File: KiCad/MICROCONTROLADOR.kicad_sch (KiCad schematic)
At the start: 18 parts, among them J3 Screw_Terminal_01x05, SW8 SW_Push, U67 PIC24HJ64GP504-I/PT, Y1 8 MHz

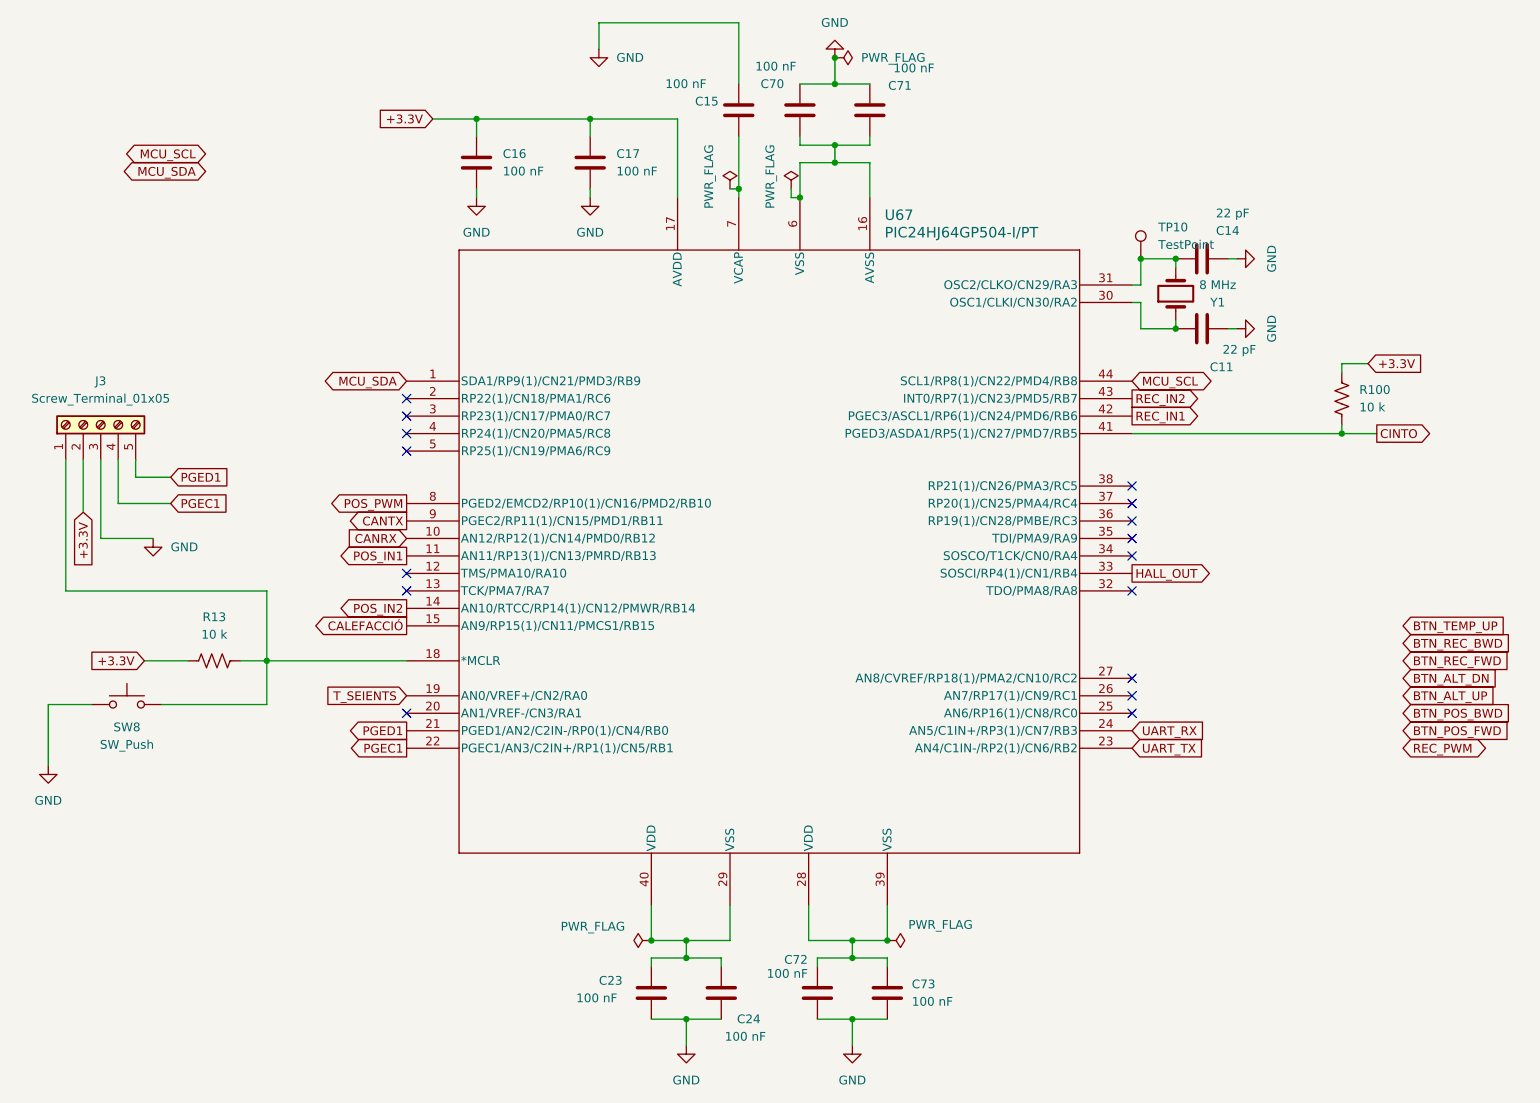
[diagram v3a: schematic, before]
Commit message: Organització Esquematic, asignacio huellas Test Points i Microcontrolador acabat
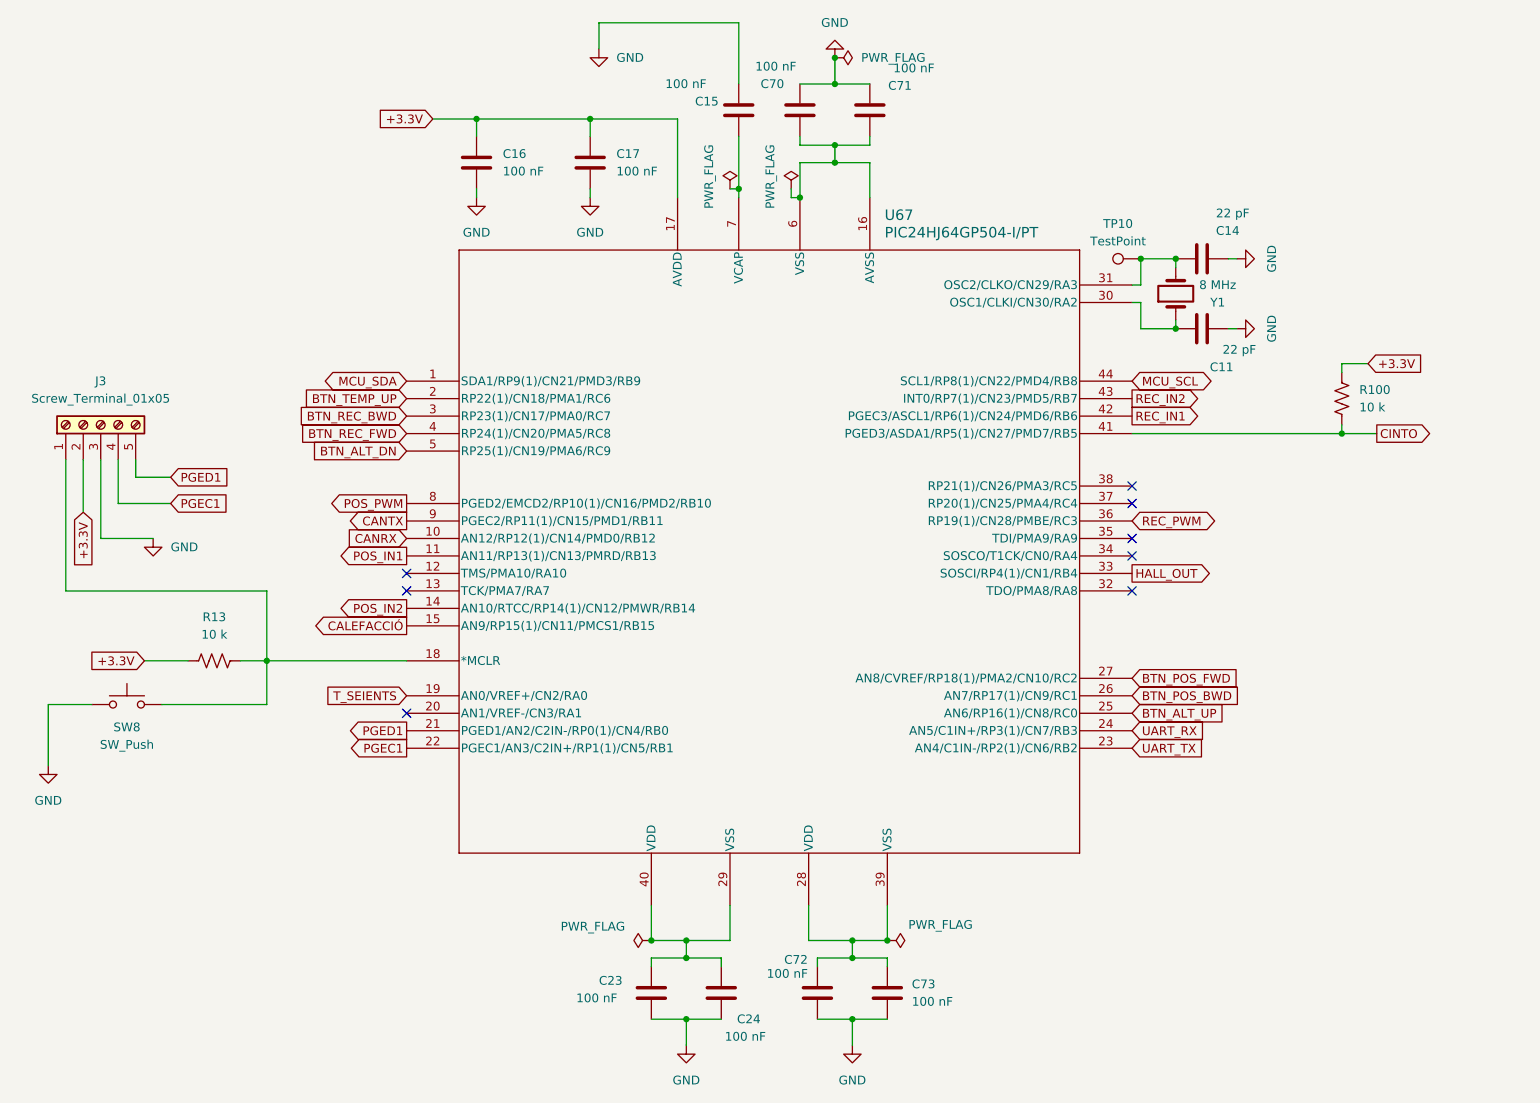
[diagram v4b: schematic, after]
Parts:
- TP10: footprint (none) -> TestPoint:TestPoint_Pad_D1.0mm
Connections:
- net BTN_ALT_DN: now also U67.5 (RP25(1)/CN19/PMA6/RC9)
- net BTN_ALT_UP: now also U67.25 (AN6/RP16(1)/CN8/RC0)
- net BTN_POS_BWD: now also U67.26 (AN7/RP17(1)/CN9/RC1)
- net BTN_POS_FWD: now also U67.27 (AN8/CVREF/RP18(1)/PMA2/CN10/RC2)
- net BTN_REC_BWD: now also U67.3 (RP23(1)/CN17/PMA0/RC7)
- net BTN_REC_FWD: now also U67.4 (RP24(1)/CN20/PMA5/RC8)
- net BTN_TEMP_UP: now also U67.2 (RP22(1)/CN18/PMA1/RC6)
- net REC_PWM: now also U67.36 (RP19(1)/CN28/PMBE/RC3)
- no-connect marks 16 -> 8
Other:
- moved on the sheet: TP10
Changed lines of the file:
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@@
 	)
 	(no_connect
-		(at 100.33 78.74)
+		(at 205.74 83.82)
+	)
+	(no_connect
+		(at 100.33 96.52)
+	)
+	(no_connect
+		(at 100.33 116.84)
 	)
 	(no_connect
@@
 	)
 	(no_connect
+		(at 205.74 93.98)
+	)
+	(no_connect
+		(at 205.74 86.36)
+	)
+	(no_connect
 		(at 100.33 99.06)
-	)
-	(no_connect
-		(at 100.33 116.84)
 	)
 	(no_connect
 		(at 205.74 99.06)
 	)
-	(no_connect
-		(at 205.74 83.82)
-	)
-	(no_connect
-		(at 205.74 86.36)
-	)
-	(no_connect
-		(at 100.33 96.52)
-	)
-	(no_connect
-		(at 205.74 114.3)
-	)
-	(no_connect
-		(at 100.33 73.66)
-	)
-	(no_connect
-		(at 100.33 76.2)
-	)
-	(no_connect
-		(at 205.74 111.76)
-	)
-	(no_connect
-		(at 205.74 116.84)
-	)
-	(no_connect
-		(at 205.74 88.9)
-	)
-	(no_connect
-		(at 100.33 71.12)
-	)
-	(no_connect
-		(at 205.74 93.98)
-	)
 	(wire
 		(pts
@@
 			(width 0)
 			(type default)
-		)
-	)
-	(global_label "MCU_SDA"
-		(shape bidirectional)
-		(at 71.12 38.1 180)
-		(fields_autoplaced yes)
-		(effects
-			(font
-				(size 1.27 1.27)
-			)
-			(justify right)
-		)
-		(property "Intersheetrefs" "${INTERSHEET_REFS}"
-			(at 58.4359 38.1 0)
-			(effects
-				(font
-					(size 1.27 1.27)
-				)
-				(justify right)
-				(hide yes)
-			)
 		)
 	)
@@
 	(global_label "BTN_POS_FWD"
 		(shape input)
-		(at 245.11 119.38 0)
+		(at 205.74 111.76 0)
 		(fields_autoplaced yes)
 		(effects
@@
 		)
 		(property "Intersheetrefs" "${INTERSHEET_REFS}"
-			(at 260.5643 119.38 0)
+			(at 221.1943 111.76 0)
 			(effects
 				(font
@@
 	(global_label "BTN_TEMP_UP"
 		(shape input)
-		(at 245.11 104.14 0)
-		(fields_autoplaced yes)
-		(effects
-			(font
-				(size 1.27 1.27)
-			)
-			(justify left)
-		)
-		(property "Intersheetrefs" "${INTERSHEET_REFS}"
-			(at 260.3828 104.14 0)
-			(effects
-				(font
-					(size 1.27 1.27)
-				)
-				(justify left)
+		(at 100.33 71.12 180)
+		(fields_autoplaced yes)
+		(effects
+			(font
+				(size 1.27 1.27)
+			)
+			(justify right)
+		)
+		(property "Intersheetrefs" "${INTERSHEET_REFS}"
+			(at 85.0572 71.12 0)
+			(effects
+				(font
+					(size 1.27 1.27)
+				)
+				(justify right)
 				(hide yes)
 			)
@@
 	(global_label "BTN_ALT_DN"
 		(shape input)
-		(at 245.11 111.76 0)
-		(fields_autoplaced yes)
-		(effects
-			(font
-				(size 1.27 1.27)
-			)
-			(justify left)
-		)
-		(property "Intersheetrefs" "${INTERSHEET_REFS}"
-			(at 258.6291 111.76 0)
-			(effects
-				(font
-					(size 1.27 1.27)
-				)
-				(justify left)
+		(at 100.33 78.74 180)
+		(fields_autoplaced yes)
+		(effects
+			(font
+				(size 1.27 1.27)
+			)
+			(justify right)
+		)
+		(property "Intersheetrefs" "${INTERSHEET_REFS}"
+			(at 86.8109 78.74 0)
+			(effects
+				(font
+					(size 1.27 1.27)
+				)
+				(justify right)
 				(hide yes)
 			)
@@
 	(global_label "BTN_REC_BWD"
 		(shape input)
-		(at 245.11 106.68 0)
-		(fields_autoplaced yes)
-		(effects
-			(font
-				(size 1.27 1.27)
-			)
-			(justify left)
-		)
-		(property "Intersheetrefs" "${INTERSHEET_REFS}"
-			(at 260.6247 106.68 0)
-			(effects
-				(font
-					(size 1.27 1.27)
-				)
-				(justify left)
+		(at 100.33 73.66 180)
+		(fields_autoplaced yes)
+		(effects
+			(font
+				(size 1.27 1.27)
+			)
+			(justify right)
+		)
+		(property "Intersheetrefs" "${INTERSHEET_REFS}"
+			(at 84.8153 73.66 0)
+			(effects
+				(font
+					(size 1.27 1.27)
+				)
+				(justify right)
 				(hide yes)
 			)
@@
 	(global_label "BTN_ALT_UP"
 		(shape input)
-		(at 245.11 114.3 0)
+		(at 205.74 116.84 0)
 		(fields_autoplaced yes)
 		(effects
@@
 		)
 		(property "Intersheetrefs" "${INTERSHEET_REFS}"
-			(at 258.6291 114.3 0)
+			(at 219.2591 116.84 0)
 			(effects
 				(font
@@
 	(global_label "REC_PWM"
 		(shape bidirectional)
-		(at 245.11 121.92 0)
+		(at 205.74 88.9 0)
 		(fields_autoplaced yes)
 		(effects
@@
 		)
 		(property "Intersheetrefs" "${INTERSHEET_REFS}"
-			(at 257.2229 121.92 0)
+			(at 217.8529 88.9 0)
 			(effects
 				(font
@@
 	(global_label "BTN_POS_BWD"
 		(shape input)
-		(at 245.11 116.84 0)
+		(at 205.74 114.3 0)
 		(fields_autoplaced yes)
 		(effects
@@
 		)
 		(property "Intersheetrefs" "${INTERSHEET_REFS}"
-			(at 260.7457 116.84 0)
+			(at 221.3757 114.3 0)
 			(effects
 				(font
@@
 		)
 	)
-	(global_label "MCU_SCL"
-		(shape bidirectional)
-		(at 71.12 35.56 180)
-		(fields_autoplaced yes)
-		(effects
-			(font
-				(size 1.27 1.27)
-			)
-			(justify right)
-		)
-		(property "Intersheetrefs" "${INTERSHEET_REFS}"
-			(at 58.4964 35.56 0)
-			(effects
-				(font
-					(size 1.27 1.27)
-				)
-				(justify right)
-				(hide yes)
-			)
-		)
-	)
 	(global_label "CINTO"
 		(shape output)
@@
 	(global_label "BTN_REC_FWD"
 		(shape input)
-		(at 245.11 109.22 0)
-		(fields_autoplaced yes)
-		(effects
-			(font
-				(size 1.27 1.27)
-			)
-			(justify left)
-		)
-		(property "Intersheetrefs" "${INTERSHEET_REFS}"
-			(at 260.4433 109.22 0)
-			(effects
-				(font
-					(size 1.27 1.27)
-				)
-				(justify left)
+		(at 100.33 76.2 180)
+		(fields_autoplaced yes)
+		(effects
+			(font
+				(size 1.27 1.27)
+			)
+			(justify right)
+		)
+		(property "Intersheetrefs" "${INTERSHEET_REFS}"
+			(at 84.9967 76.2 0)
+			(effects
+				(font
+					(size 1.27 1.27)
+				)
+				(justify right)
 				(hide yes)
 			)
@@
 	(symbol
 		(lib_id "Connector:TestPoint")
-		(at 207.01 50.8 0)
+		(at 207.01 50.8 90)
 		(unit 1)
 		(exclude_from_sim no)
@@
 		(fields_autoplaced yes)
 		(property "Reference" "TP10"
-			(at 209.55 46.2279 0)
-			(effects
-				(font
-					(size 1.27 1.27)
-				)
-				(justify left)
+			(at 203.708 45.72 90)
+			(effects
+				(font
+					(size 1.27 1.27)
+				)
 			)
 		)
 		(property "Value" "TestPoint"
-			(at 209.55 48.7679 0)
-			(effects
-				(font
-					(size 1.27 1.27)
-				)
-				(justify left)
-			)
-		)
-		(property "Footprint" ""
-			(at 212.09 50.8 0)
+			(at 203.708 48.26 90)
+			(effects
+				(font
+					(size 1.27 1.27)
+				)
+			)
+		)
+		(property "Footprint" "TestPoint:TestPoint_Pad_D1.0mm"
+			(at 207.01 45.72 0)
 			(effects
 				(font
@@
 		)
 		(property "Datasheet" "~"
-			(at 212.09 50.8 0)
-			(effects
-				(font
+			(at 207.01 45.72 0)
+			(effects
+				(font

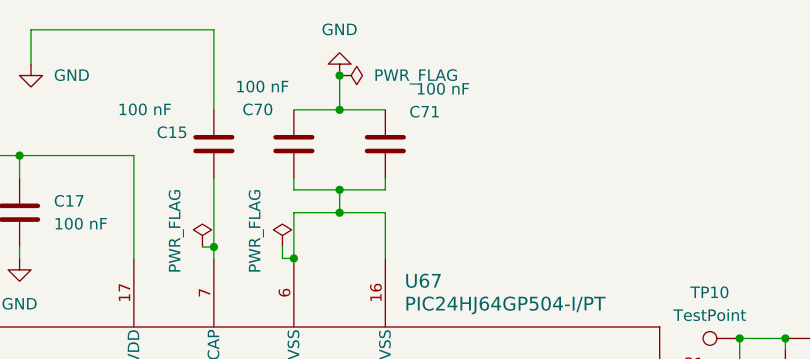
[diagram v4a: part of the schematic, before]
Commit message: Modificació d'errors varis
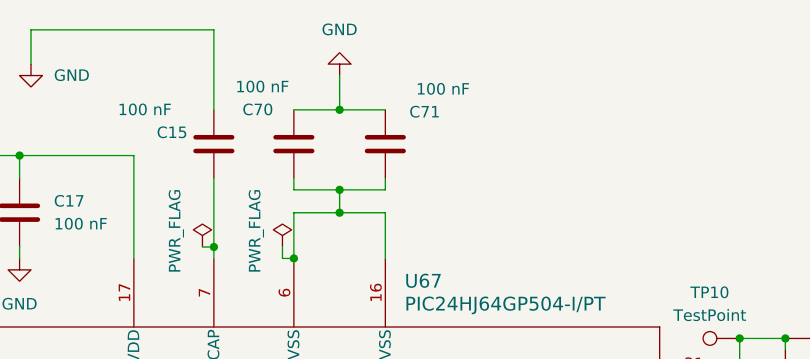
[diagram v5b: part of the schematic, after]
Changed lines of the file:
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@@
-	)
-	(junction
-		(at 162.56 21.59)
-		(diameter 0)
-		(color 0 0 0 0)
 	)
 	(junction
@@
 					(unit 1)
 				)
-			)
-		)
-	)
-	(symbol
-		(lib_id "power:PWR_FLAG")
-		(at 162.56 21.59 270)
-		(unit 1)
-		(exclude_from_sim no)
-		(in_bom yes)
-		(on_board yes)
-		(dnp no)
-		(fields_autoplaced yes)
-		(property "Reference" "#FLG0101"
-			(at 164.465 21.59 0)
-			(effects
-				(font
-					(size 1.27 1.27)
-				)
-				(hide yes)
-			)
-		)
-		(property "Value" "PWR_FLAG"
-			(at 166.37 21.5901 90)
-			(effects
-				(font
-					(size 1.27 1.27)
-				)
-				(justify left)
-			)
-		)
-		(property "Footprint" ""
-			(at 162.56 21.59 0)
-			(effects
-				(font
-					(size 1.27 1.27)
-				)
-				(hide yes)
-			)
-		)
-		(property "Datasheet" "~"
-			(at 162.56 21.59 0)
-			(effects
-				(font
-					(size 1.27 1.27)
-				)
-				(hide yes)
-			)
-		)
-		(property "Description" "Special symbol for telling ERC where power comes from"
-			(at 162.56 21.59 0)
-			(effects
-				(font
-					(size 1.27 1.27)
-				)
-				(hide yes)
-			)
-		)
-		(pin "1"
-		)
-		(instances
-			(project "MICROCONTROLADOR"
-				(path "/9b2329e0-99c8-4c5f-bbda-c735127483a8"
-					(reference "#FLG0102")
-					(unit 1)
-				)
-			)
-			(project "SEIENTS_EDD"
-				(path "/b6401b4f-5426-49b8-bb2e-8ecdb19989ef/2352108e-71c7-4bd2-90ee-aa6ba1d65197"
-					(reference "#FLG0101")
-					(unit 1)
-				)

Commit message: Modificació al routing
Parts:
- C16: footprint Capacitor_THT:C_Disc_D5.0mm_W2.5mm_P5.00mm -> Capacitor_SMD:C_0805_2012Metric
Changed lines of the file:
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@@
 			)
 		)
-		(property "Footprint" "Capacitor_THT:C_Disc_D5.0mm_W2.5mm_P5.00mm"
+		(property "Footprint" "Capacitor_SMD:C_0805_2012Metric"
 			(at 111.4552 40.64 0)
 			(effects

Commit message: ROUTING FINAL
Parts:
- removed C24, C70, C71, C72, C73: 100 nF, Capacitor_SMD:C_0805_2012Metric, symbol Device:C
- added C7: 100 nF, Capacitor_SMD:C_0805_2012Metric, symbol Device:C
- C15: value 100 nF -> 2.2 uF
- C17: value 100 nF -> 1uF
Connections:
- net BTN_ALT_DN: now also U67.38 (RP21(1)/CN26/PMA3/RC5); no longer U67.5 (RP25(1)/CN19/PMA6/RC9)
- net BTN_ALT_UP: now also U67.32 (TDO/PMA8/RA8); no longer U67.25 (AN6/RP16(1)/CN8/RC0)
- net BTN_POS_BWD: now also U67.33 (SOSCI/RP4(1)/CN1/RB4); no longer U67.26 (AN7/RP17(1)/CN9/RC1)
- net BTN_POS_FWD: now also U67.34 (SOSCO/T1CK/CN0/RA4); no longer U67.27 (AN8/CVREF/RP18(1)/PMA2/CN10/RC2)
- net BTN_REC_BWD: now also U67.36 (RP19(1)/CN28/PMBE/RC3); no longer U67.3 (RP23(1)/CN17/PMA0/RC7)
- net BTN_REC_FWD: now also U67.37 (RP20(1)/CN25/PMA4/RC4); no longer U67.4 (RP24(1)/CN20/PMA5/RC8)
- net BTN_TEMP_UP: now also U67.35 (TDI/PMA9/RA9); no longer U67.2 (RP22(1)/CN18/PMA1/RC6)
- net CALEFACCIÓ: now also U67.43 (INT0/RP7(1)/CN23/PMD5/RB7); no longer U67.15 (AN9/RP15(1)/CN11/PMCS1/RB15)
- net CANRX: now also U67.14 (AN10/RTCC/RP14(1)/CN12/PMWR/RB14); no longer U67.10 (AN12/RP12(1)/CN14/PMD0/RB12)
- net CANTX: now also U67.15 (AN9/RP15(1)/CN11/PMCS1/RB15); no longer U67.9 (PGEC2/RP11(1)/CN15/PMD1/RB11)
- net GND: now also C15.1, U67.16 (AVSS), U67.29 (VSS), U67.39 (VSS), U67.6 (VSS), C7.2; no longer C15.2
- net HALL_OUT: now also U67.42 (PGEC3/ASCL1/RP6(1)/CN24/PMD6/RB6); no longer U67.33 (SOSCI/RP4(1)/CN1/RB4)
- net PGEC1: now also J3.5 (Pin_5); no longer J3.4 (Pin_4)
- net PGED1: now also J3.4 (Pin_4); no longer J3.5 (Pin_5)
- net POS_IN1: now also U67.3 (RP23(1)/CN17/PMA0/RC7); no longer U67.11 (AN11/RP13(1)/CN13/PMRD/RB13)
- net POS_IN2: now also U67.4 (RP24(1)/CN20/PMA5/RC8); no longer U67.14 (AN10/RTCC/RP14(1)/CN12/PMWR/RB14)
- net POS_PWM: now also U67.2 (RP22(1)/CN18/PMA1/RC6); no longer U67.8 (PGED2/EMCD2/RP10(1)/CN16/PMD2/RB10)
- net REC_IN1: now also U67.5 (RP25(1)/CN19/PMA6/RC9); no longer U67.42 (PGEC3/ASCL1/RP6(1)/CN24/PMD6/RB6)
- net REC_IN2: now also U67.8 (PGED2/EMCD2/RP10(1)/CN16/PMD2/RB10); no longer U67.43 (INT0/RP7(1)/CN23/PMD5/RB7)
- net REC_PWM: now also U67.9 (PGEC2/RP11(1)/CN15/PMD1/RB11); no longer U67.36 (RP19(1)/CN28/PMBE/RC3)
- net T_SEIENTS: now also U67.27 (AN8/CVREF/RP18(1)/PMA2/CN10/RC2); no longer U67.19 (AN0/VREF+/CN2/RA0)
- net at C23.1, U67.40 (VDD): no longer U67.29 (VSS)
- net at U67.28 (VDD): now also C7.1; no longer U67.39 (VSS)
- net at U67.7 (VCAP): now also C15.2; no longer C15.1
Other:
- moved on the sheet: C11, C14, C15, C16, C17, C23, R100, SW8, Y1

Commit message: Layout acabado
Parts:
- C15: footprint Capacitor_THT:C_Disc_D5.0mm_W2.5mm_P5.00mm -> Capacitor_SMD:C_0805_2012Metric
- C17: footprint Capacitor_THT:C_Disc_D3.0mm_W1.6mm_P2.50mm -> Capacitor_SMD:C_0805_2012Metric
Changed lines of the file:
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@@
 			)
 		)
-		(property "Footprint" "Capacitor_THT:C_Disc_D5.0mm_W2.5mm_P5.00mm"
+		(property "Footprint" "Capacitor_SMD:C_0805_2012Metric"
 			(at 140.6652 34.29 0)
 			(effects
@@
 			)
 		)
-		(property "Footprint" "Capacitor_THT:C_Disc_D3.0mm_W1.6mm_P2.50mm"
+		(property "Footprint" "Capacitor_SMD:C_0805_2012Metric"
 			(at 119.0752 40.64 0)
 			(effects
